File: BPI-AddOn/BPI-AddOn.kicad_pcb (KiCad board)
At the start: 2 copper layers, 100 x 100 mm, 73 parts, among them CON1 BARREL_JACK, J1 RJ45, J2 RJ45, J3 RJ45, P1 DIN10-1, P10 CONN_01X03, P11 CONN_01X05, P12 CONN_01X05, P13 CONN_01X08, P15 CONN_02X11, P16 USB_B, P17 CONN_01X05, P18 CONN_01X05, P19 V, P2 DIN10-2, P20 - +, P21 USB_OTG, P22 CONN_01X06, P23 CONN_01X06, P24 CONN_02X02, P25 CONN_01X02, P3 DIN10-3, P4 DIN10-4, P5 DIN10-5, P6 DIN7-1, P7 DIN7-2, P8 DIN7-3, P9 CONN_01X03, U1 MC34063, U2 FT230XS

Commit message: wip
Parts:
- F1, F2: footprint Fuse_Holders_and_Fuses:BladeFuse-Mini -> w_capacitors:cnp_6mm_disc
- moved D4 7.44 mm to (99.0, 77.6)
- moved F2 5.24 mm to (90.2, 79.1)
- moved F1 4.68 mm to (90.3, 73.3)
- moved DCDC1 3.70 mm to (91.7, 96.1)
- moved R13 2.04 mm to (95.6, 76.8)
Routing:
- net /CANH: track 0.00 -> 26.5 mm
- net /CANL: track 0.00 -> 26.1 mm
- net Net-(J3-Pad1): track 0.00 -> 15.9 mm
- net Net-(J3-Pad7): track 0.00 -> 14.2 mm
- net Net-(J3-Pad3): track 0.00 -> 14.2 mm
- net Net-(J3-Pad5): track 0.00 -> 13.2 mm
- net Net-(J3-Pad2): track 0.00 -> 13.1 mm
- net Net-(J3-Pad8): track 0.00 -> 13.0 mm
- net VCC: track 0.00 -> 11.7 mm
- net Net-(J3-Pad6): track 0.00 -> 11.2 mm
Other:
- net class Defaul_II added: clearance 0.2, trace_width 0.6, via_dia 1, via_drill 0.8
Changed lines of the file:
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@@
   (general
     (links 234)
-    (no_connects 234)
+    (no_connects 220)
     (area 66.924999 48.924999 167.075001 149.075001)
     (thickness 1.6)
     (drawings 74)
-    (tracks 0)
+    (tracks 32)
     (zones 0)
     (modules 73)
@@
     (uvia_dia 0.3)
     (uvia_drill 0.1)
+  )
+  (net_class Defaul_II ""
+    (clearance 0.2)
+    (trace_width 0.6)
+    (via_dia 1)
+    (via_drill 0.8)
+    (uvia_dia 0.6)
+    (uvia_drill 0.2)
     (add_net /5V)
     (add_net /CANH)
@@
     )
   )
-  (module Fuse_Holders_and_Fuses:BladeFuse-Mini (layer F.Cu)
-    (at 89 77.8)
-    (fp_text reference F1 (at 0.2 -4.7) (layer F.SilkS)
-      (effects (font (size 1 1) (thickness 0.15)))
-    )
-    (fp_text value FUSE (at 0.2 4.7) (layer F.Fab)
-      (effects (font (size 1 1) (thickness 0.15)))
-    )
-    (fp_line (start -0.75 0) (end 0.85 0) (layer F.SilkS) (width 0.15))
-    (fp_line (start 1.6 2) (end -1.6 2) (layer F.SilkS) (width 0.15))
-    (fp_line (start -1.6 -2) (end 1.6 -2) (layer F.SilkS) (width 0.15))
-    (pad 1 thru_hole oval (at -4 0) (size 5.5 3.8) (drill oval 3.5 2) (layers *.Cu *.Mask F.SilkS)
-      (net 10 /5V))
-    (pad 2 thru_hole oval (at 4 0) (size 5.3 3.8) (drill oval 3.5 2) (layers *.Cu *.Mask F.SilkS)
-      (net 12 "Net-(F1-Pad2)"))
-    (model Fuse_Holders_and_Fuses.3dshapes/BladeFuse-Mini.wrl
-      (at (xyz 0 0 0))
-      (scale (xyz 0.3937 0.3937 0.3937))
-      (rotate (xyz 0 0 0))
-    )
-  )
-  (module Fuse_Holders_and_Fuses:BladeFuse-Mini (layer F.Cu)
-    (at 89 84.2 180)
-    (fp_text reference F2 (at 0.2 -4.7 180) (layer F.SilkS)
-      (effects (font (size 1 1) (thickness 0.15)))
-    )
-    (fp_text value FUSE (at 0.2 4.7 180) (layer F.Fab)
-      (effects (font (size 1 1) (thickness 0.15)))
-    )
-    (fp_line (start -0.75 0) (end 0.85 0) (layer F.SilkS) (width 0.15))
-    (fp_line (start 1.6 2) (end -1.6 2) (layer F.SilkS) (width 0.15))
-    (fp_line (start -1.6 -2) (end 1.6 -2) (layer F.SilkS) (width 0.15))
-    (pad 1 thru_hole oval (at -4 0 180) (size 5.5 3.8) (drill oval 3.5 2) (layers *.Cu *.Mask F.SilkS)
-      (net 13 "Net-(F2-Pad1)"))
-    (pad 2 thru_hole oval (at 4 0 180) (size 5.3 3.8) (drill oval 3.5 2) (layers *.Cu *.Mask F.SilkS)
-      (net 14 /Vdd))
-    (model Fuse_Holders_and_Fuses.3dshapes/BladeFuse-Mini.wrl
-      (at (xyz 0 0 0))
-      (scale (xyz 0.3937 0.3937 0.3937))
-      (rotate (xyz 0 0 0))
-    )
-  )
   (module w_conn_pc:megb8-8 (layer F.Cu)
     (at 144.5 146)
@@
     (at 144 118)
     (descr "USB B mini SMD connector")
-    (fp_text reference P21 (at 0 6.10108) (layer F.SilkS)
+    (fp_text reference P21 (at 0 1.9) (layer F.SilkS)
       (effects (font (size 0.99822 0.99822) (thickness 0.19558)))
     )
-    (fp_text value USB_OTG (at 0 -5.90042) (layer F.SilkS)
+    (fp_text value USB_OTG (at 0 0.2) (layer F.SilkS)
       (effects (font (size 0.99822 0.99822) (thickness 0.19812)))
     )
@@
   )
   (module LEDs:LED-5MM (layer F.Cu)
-    (at 99.8 85)
+    (at 99 77.6)
     (descr "LED 5mm round vertical")
     (tags "LED 5mm round vertical")
@@
   )
   (module w_pth_resistors:RC03 (layer F.Cu)
-    (at 97.6 76.4 90)
+    (at 95.6 76.8 90)
     (descr "Resistor, RC03")
     (tags R)
@@
   )
   (module 78xx:DCDC (layer F.Cu)
-    (at 91.8 99.8)
+    (at 91.7 96.1)
     (descr "DC-DC Board")
     (tags DCDC)
@@
     (pad 8 thru_hole oval (at 6.604 9.271) (size 1.6 1.6) (drill 0.8) (layers *.Cu *.Mask F.SilkS)
       (net 5 GNDA))
+  )
+  (module w_capacitors:cnp_6mm_disc (layer F.Cu)
+    (at 90.3 73.3)
+    (descr "6mm disc ceramic capacitor")
+    (tags C)
+    (fp_text reference F1 (at 0 -3.81) (layer F.SilkS)
+      (effects (font (size 1.016 1.016) (thickness 0.2032)))
+    )
+    (fp_text value FUSE (at 0 -2.286) (layer F.SilkS) hide
+      (effects (font (size 1.016 1.016) (thickness 0.2032)))
+    )
+    (fp_line (start -3.048 -0.889) (end -3.048 0.889) (layer F.SilkS) (width 0.24892))
+    (fp_line (start -3.048 0.889) (end 3.048 0.889) (layer F.SilkS) (width 0.24892))
+    (fp_line (start 3.048 0.889) (end 3.048 -0.889) (layer F.SilkS) (width 0.24892))
+    (fp_line (start 3.048 -0.889) (end -3.048 -0.889) (layer F.SilkS) (width 0.24892))
+    (pad 1 thru_hole circle (at -2.54 0) (size 1.50114 1.50114) (drill 0.8001) (layers *.Cu *.Mask F.SilkS)
+      (net 10 /5V))
+    (pad 2 thru_hole circle (at 2.54 0) (size 1.50114 1.50114) (drill 0.8001) (layers *.Cu *.Mask F.SilkS)
+      (net 12 "Net-(F1-Pad2)"))
+    (model walter/capacitors/cnp_6mm_disc.wrl
+      (at (xyz 0 0 0))
+      (scale (xyz 1 1 1))
+      (rotate (xyz 0 0 0))
+    )
+  )
+  (module w_capacitors:cnp_6mm_disc (layer F.Cu)
+    (at 90.2 79.1 180)
+    (descr "6mm disc ceramic capacitor")
+    (tags C)
+    (fp_text reference F2 (at 0 -3.81 180) (layer F.SilkS)
+      (effects (font (size 1.016 1.016) (thickness 0.2032)))
+    )
+    (fp_text value FUSE (at 0 -2.286 180) (layer F.SilkS) hide
+      (effects (font (size 1.016 1.016) (thickness 0.2032)))
+    )
+    (fp_line (start -3.048 -0.889) (end -3.048 0.889) (layer F.SilkS) (width 0.24892))
+    (fp_line (start -3.048 0.889) (end 3.048 0.889) (layer F.SilkS) (width 0.24892))
+    (fp_line (start 3.048 0.889) (end 3.048 -0.889) (layer F.SilkS) (width 0.24892))
+    (fp_line (start 3.048 -0.889) (end -3.048 -0.889) (layer F.SilkS) (width 0.24892))
+    (pad 1 thru_hole circle (at -2.54 0 180) (size 1.50114 1.50114) (drill 0.8001) (layers *.Cu *.Mask F.SilkS)
+      (net 13 "Net-(F2-Pad1)"))
+    (pad 2 thru_hole circle (at 2.54 0 180) (size 1.50114 1.50114) (drill 0.8001) (layers *.Cu *.Mask F.SilkS)
+      (net 14 /Vdd))
+    (model walter/capacitors/cnp_6mm_disc.wrl
+      (at (xyz 0 0 0))
+      (scale (xyz 1 1 1))
+      (rotate (xyz 0 0 0))
+    )
   )
   (gr_text BR (at 137.6 131.1 90) (layer F.SilkS)
@@
   (gr_line (start 69.5 149) (end 114.5 149) (angle 90) (layer Edge.Cuts) (width 0.15))
   (gr_line (start 69.5 49) (end 114.5 49) (angle 90) (layer Edge.Cuts) (width 0.15))
+  (segment (start 88.09 129.75) (end 88.09 120) (width 0.6) (layer B.Cu) (net 2))
+  (segment (start 88.09 133.25) (end 88.09 129.75) (width 0.6) (layer B.Cu) (net 2))
+  (segment (start 84 144.8) (end 84 140.9) (width 0.6) (layer B.Cu) (net 2))
+  (segment (start 88.09 136.81) (end 88.09 133.25) (width 0.6) (layer B.Cu) (net 2))
+  (segment (start 84 140.9) (end 88.09 136.81) (width 0.6) (layer B.Cu) (net 2))
+  (segment (start 90.63 129.75) (end 90.63 120) (width 0.6) (layer B.Cu) (net 3))
+  (segment (start 90.63 133.25) (end 90.63 129.75) (width 0.6) (layer B.Cu) (net 3))
+  (segment (start 87.5 144.8) (end 87.5 140.5) (width 0.6) (layer B.Cu) (net 3))
+  (segment (start 90.63 137.37) (end 90.63 133.25) (width 0.6) (layer B.Cu) (net 3))
+  (segment (start 87.5 140.5) (end 90.63 137.37) (width 0.6) (layer B.Cu) (net 3))
+  (segment (start 142.595 139.66) (end 142.595 136.195) (width 0.6) (layer B.Cu) (net 15))
+  (segment (start 140.08 133.68) (end 140.08 126.5) (width 0.6) (layer B.Cu) (net 15))
+  (segment (start 142.595 136.195) (end 140.08 133.68) (width 0.6) (layer B.Cu) (net 15))
+  (segment (start 140.055 139.66) (end 138.96 139.66) (width 0.6) (layer B.Cu) (net 16))
+  (segment (start 135 135.7) (end 135 126.5) (width 0.6) (layer B.Cu) (net 16))
+  (segment (start 138.96 139.66) (end 135 135.7) (width 0.6) (layer B.Cu) (net 16))
+  (segment (start 141.325 137.12) (end 139.82 137.12) (width 0.6) (layer B.Cu) (net 17))
+  (segment (start 137.54 134.84) (end 137.54 126.5) (width 0.6) (layer B.Cu) (net 17))
+  (segment (start 139.82 137.12) (end 137.54 134.84) (width 0.6) (layer B.Cu) (net 17))
+  (segment (start 145.135 139.66) (end 145.135 126.525) (width 0.6) (layer B.Cu) (net 19))
+  (segment (start 145.135 126.525) (end 145.16 126.5) (width 0.6) (layer B.Cu) (net 19))
+  (segment (start 146.405 137.12) (end 146.405 134.795) (width 0.6) (layer B.Cu) (net 20))
+  (segment (start 147.7 133.5) (end 147.7 126.5) (width 0.6) (layer B.Cu) (net 20))
+  (segment (start 146.405 134.795) (end 147.7 133.5) (width 0.6) (layer B.Cu) (net 20))
+  (segment (start 150.24 126.5) (end 150.24 132.96) (width 0.6) (layer B.Cu) (net 21))
+  (segment (start 147.675 135.525) (end 147.675 139.66) (width 0.6) (layer B.Cu) (net 21))
+  (segment (start 150.24 132.96) (end 147.675 135.525) (width 0.6) (layer B.Cu) (net 21))
+  (segment (start 148.945 137.12) (end 150.38 137.12) (width 0.6) (layer B.Cu) (net 22))
+  (segment (start 152.78 134.72) (end 152.78 126.5) (width 0.6) (layer B.Cu) (net 22))
+  (segment (start 150.38 137.12) (end 152.78 134.72) (width 0.6) (layer B.Cu) (net 22))
+  (segment (start 98 144.8) (end 98 133.5) (width 0.6) (layer B.Cu) (net 24))
+  (segment (start 98 133.5) (end 98.25 133.25) (width 0.6) (layer B.Cu) (net 24))
 )

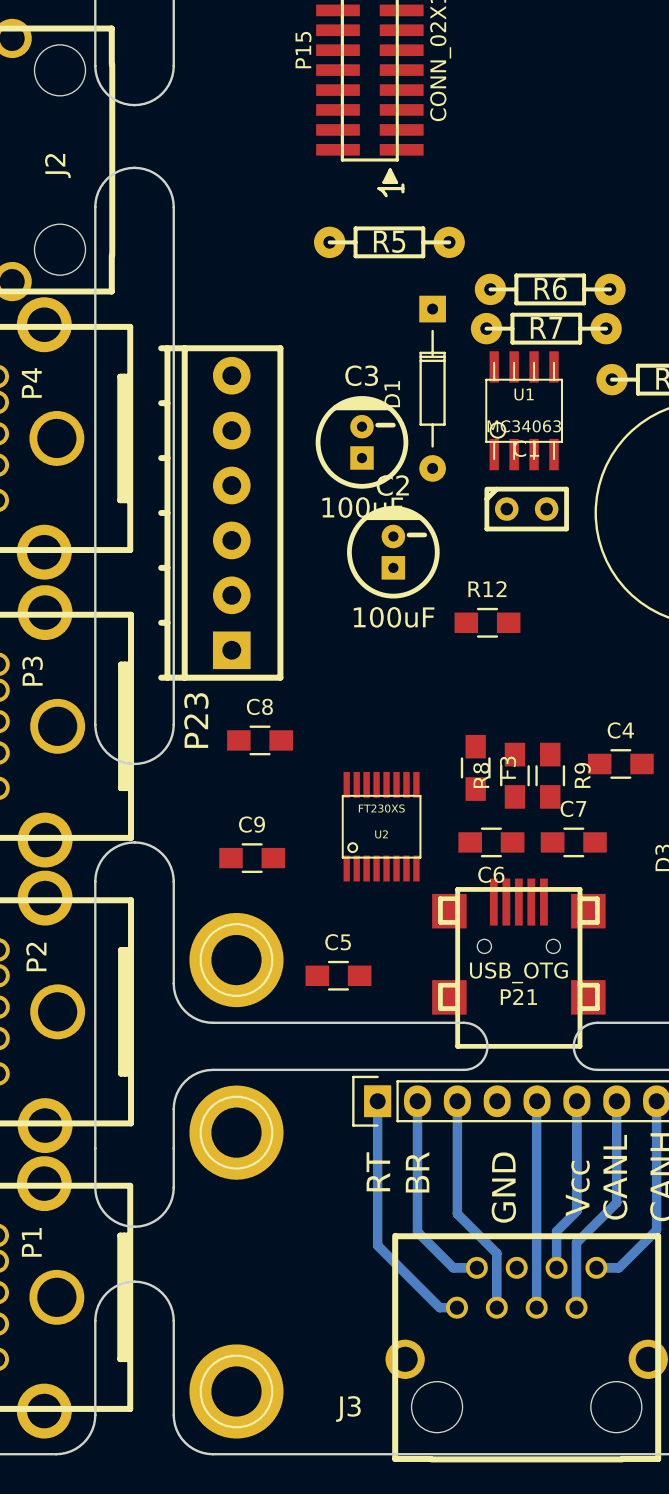
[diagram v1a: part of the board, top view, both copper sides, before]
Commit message: add breaking points
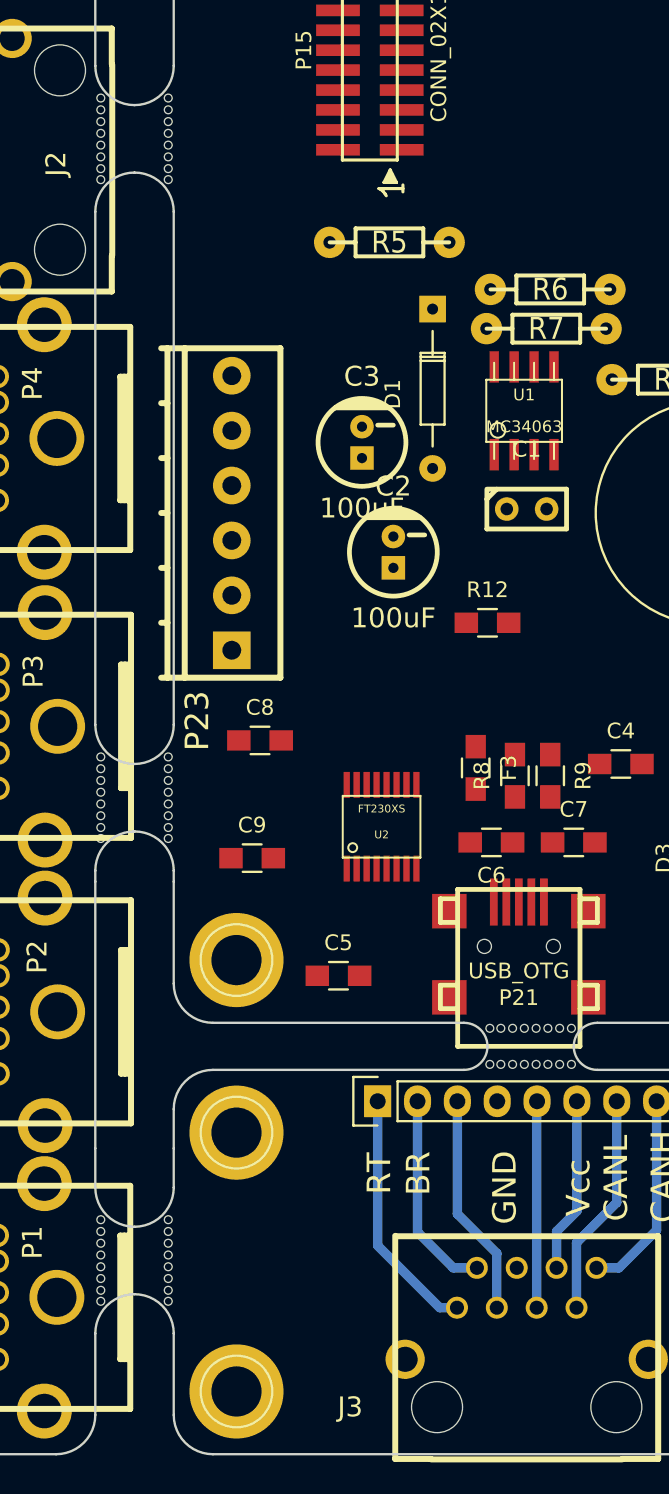
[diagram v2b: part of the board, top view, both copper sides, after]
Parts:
- added E05: abortedge, maerklin:abortedge, F.Cu at (145.1, 122.9)
- added E05: abortedge, maerklin:abortedge, F.Cu at (145.1, 120.6)
- added E05: abortedge, maerklin:abortedge, F.Cu at (120.4, 136.3)
- added E05: abortedge, maerklin:abortedge, F.Cu at (116.1, 136.3)
- added E05: abortedge, maerklin:abortedge, F.Cu at (120.4, 106.8)
- added E05: abortedge, maerklin:abortedge, F.Cu at (116.1, 106.8)
- added E05: abortedge, maerklin:abortedge, F.Cu at (120.4, 64.8)
- added E05: abortedge, maerklin:abortedge, F.Cu at (116.1, 64.8)
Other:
- outline, holes or cut-outs redrawn

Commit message: routing ...
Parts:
- moved C8 10.5 mm to (134.7, 111.2)
- moved C9 9.73 mm to (134.7, 117.0)
- moved D2 6.55 mm to (154.0, 116.5), turned to 270 degrees
- moved D3 5.74 mm to (156.5, 116.5), turned to 270 degrees
- moved R10 4.92 mm to (154.0, 112.0), turned to 90 degrees
- moved C5 4.84 mm to (134.6, 114.1)
- moved R11 3.77 mm to (156.5, 112.0), turned to 90 degrees
- moved U2 3.47 mm to (135.7, 105.6)
- moved F2 3.41 mm to (88.1, 76.4)
- moved R3 2.51 mm to (84.8, 124.2)
- moved D4 2.39 mm to (98.2, 75.3), turned to 270 degrees
- moved F1 2.30 mm to (88.0, 73.0)
- moved C4 2.30 mm to (149.8, 107.2)
- moved R13 2.28 mm to (93.3, 76.8)
- moved P25 1.25 mm to (82.0, 127.1)
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- renumbered F3 to F
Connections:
- net Net-(J3-Pad4) renamed /GNDB
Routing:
- net /CANH: track 26.5 -> 106.0 mm, vias 0 -> 1
- net /CANL: track 26.1 -> 101.3 mm, vias 0 -> 1
- net /5V: track 0.00 -> 12.4 mm
- net VCC: track 11.7 -> 0.35 mm
- added copper zone on B.Cu, net /GNDB
- added copper zone on F.Cu, net /GNDB
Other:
- board text added: "(BR)"
- board text added: "(RT)"
- board text removed: "BR"
- board text removed: "RT"

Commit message: ip
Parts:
- moved R13 3.11 mm to (93.5, 79.9)
- moved F2 2.97 mm to (87.6, 79.4)
- moved F1 2.78 mm to (87.9, 75.8)
- moved D4 1.66 mm to (98.6, 77.0)
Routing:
- net VCC: track 0.35 -> 130.6 mm, vias 0 -> 1
- net /5V: track 12.4 -> 77.9 mm
- net /CANL: track 101.3 -> 146.0 mm, vias 1 -> 3
- net /CANH: track 106.0 -> 149.1 mm, vias 1 -> 3
- net /J2_V: track 0.00 -> 10.8 mm
- net /J1_V: track 0.00 -> 10.4 mm
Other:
- net class Vcc added: clearance 0.2, trace_width 1.2, via_dia 2, via_drill 1.6
